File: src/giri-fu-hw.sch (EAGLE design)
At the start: 30 parts, among them IC1 ATMEGA168-20P, IC2 7805T, IC3 ULN2003AN, K1 G5V1, K2 G5V1, K3 G5V1, K4 G5V1, K5 G5V1, K6 G5V1, Q1 16MHz

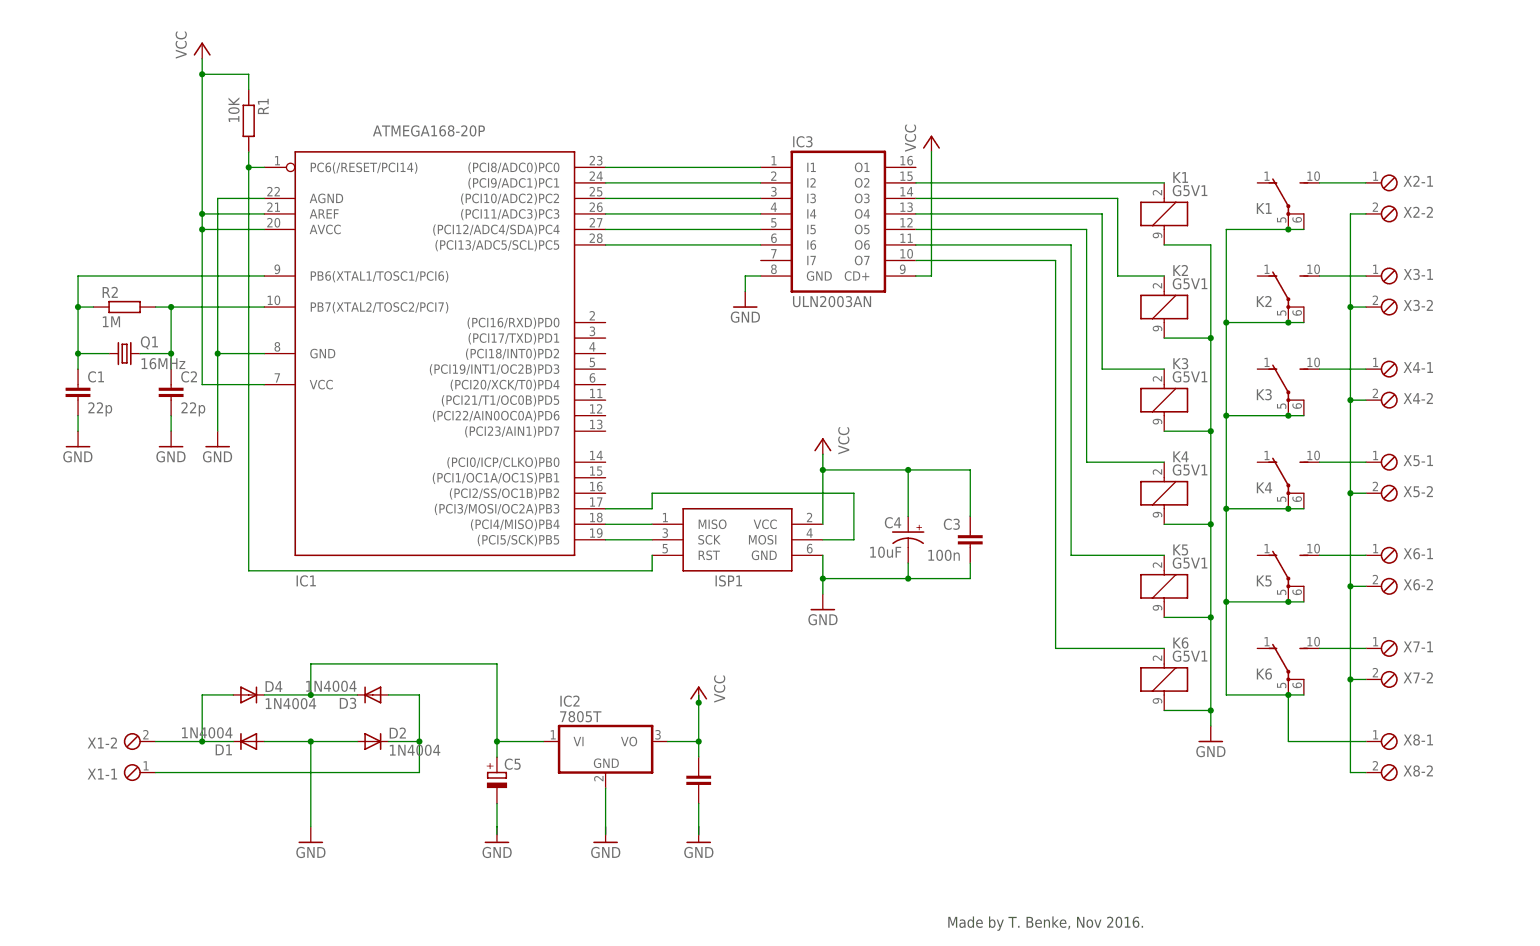
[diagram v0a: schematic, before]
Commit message: Add Schematics Add PCB board design Add top and bottom prints for manual PCB manufacturing Add partlist Add photo on the prototype board Add datasheet to the RYS-5 relay
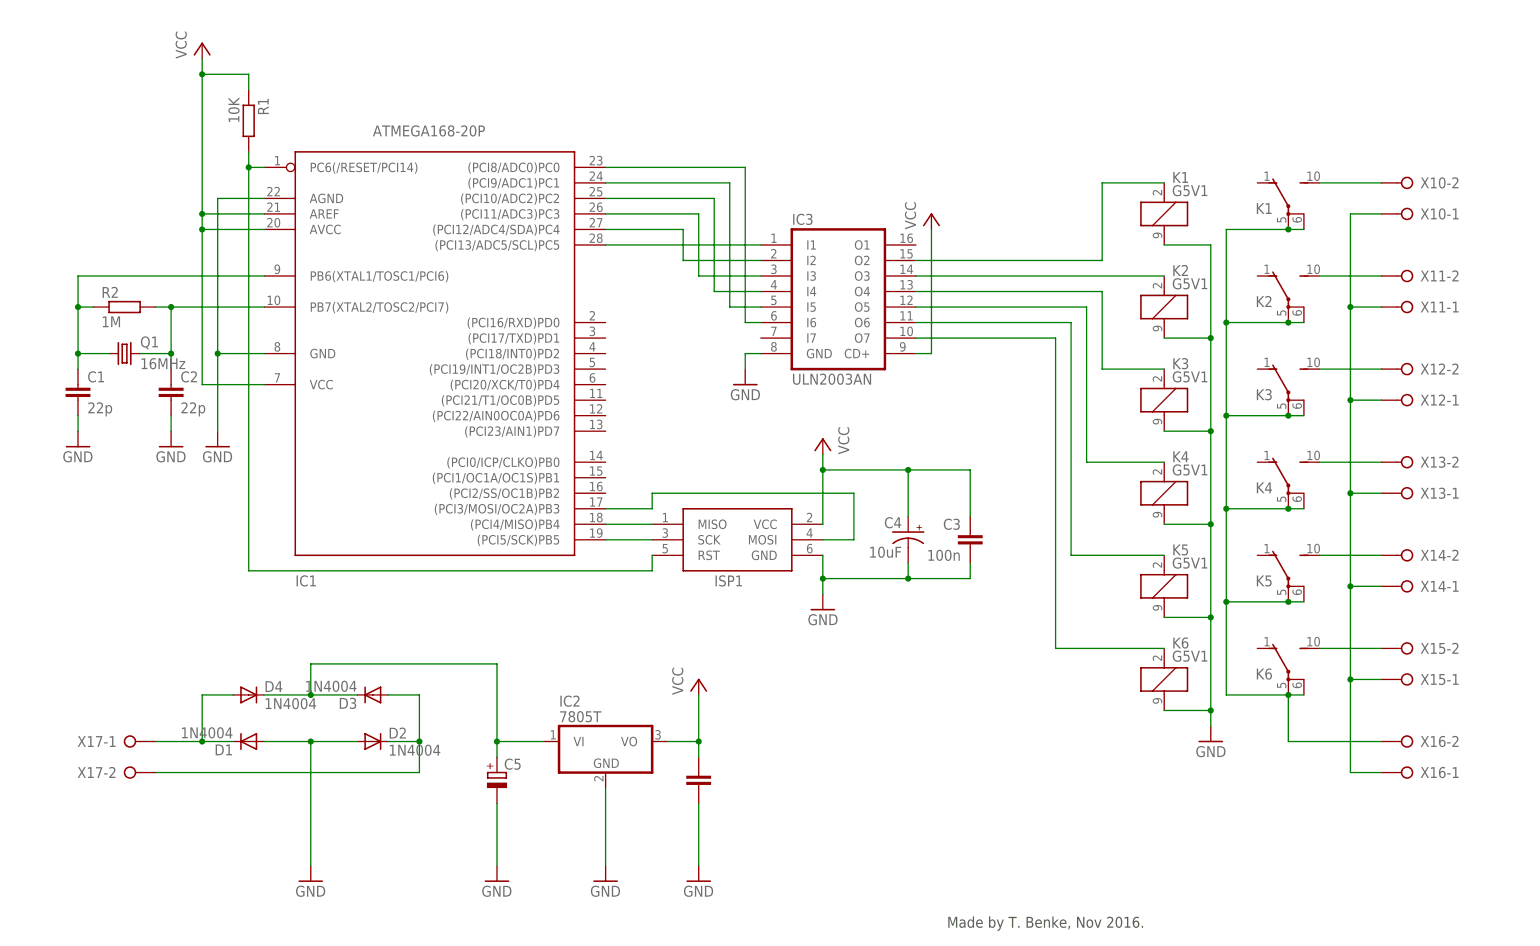
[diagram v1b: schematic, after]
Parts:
- removed X1, X2, X3, X4, X5, X6, X7, X8: (no value), con-phoenix-254:MPT2
- added X10, X11, X12, X13, X14, X15, X16, X17: (no value), con-wago-508:W237-02P
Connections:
- removed net N$24: IC2.GND
- removed net N$25: C5.-
- removed net N$26: IC2.VO
- removed net N$8: IC1.(PCI13/ADC5/SCL)PC5, IC3.I6
- net GND: now also C5.-, D1.A, D2.A, IC2.GND
- net N$1: now also IC3.I6; no longer IC3.I1
- net N$2: now also IC1.(PCI9/ADC1)PC1, IC3.I5; no longer D1.A, D2.A
- net N$22: now also X17-1.KL; no longer X1-2.1
- net N$23: now also X17-2.KL; no longer X1-1.1
- net N$28: now also X10-2.KL; no longer X2-1.1
- net N$29: now also X11-2.KL; no longer X3-1.1
- net N$3: now also X16-2.KL; no longer X8-1.1
- net N$30: now also X12-2.KL; no longer X4-1.1
- net N$31: now also X13-2.KL; no longer X5-1.1
- net N$32: now also X14-2.KL; no longer X6-1.1
- net N$33: now also X15-2.KL; no longer X7-1.1
- net N$35: now also X10-1.KL, X11-1.KL, X12-1.KL, X13-1.KL, X14-1.KL, X15-1.KL, X16-1.KL; no longer X2-2.1, X3-2.1, X4-2.1, X5-2.1, X6-2.1, X7-2.1, X8-2.1
- net N$4: now also IC1.(PCI10/ADC2)PC2, IC3.I4; no longer IC1.(PCI9/ADC1)PC1, IC3.I2
- net N$5: now also IC1.(PCI13/ADC5/SCL)PC5, IC3.I1; no longer IC1.(PCI10/ADC2)PC2, IC3.I3
- net N$6: now also IC3.I3; no longer IC3.I4
- net N$7: now also IC3.I2; no longer IC3.I5
- net VCC: now also IC2.VO
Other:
- moved on the sheet: IC3

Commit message: Rename inputs and outputs Regenerate dist artifacts
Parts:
- renumbered X10 to SWITCH_1, X11 to SWITCH_2, X12 to SWITCH_3, X13 to SWITCH_4, X14 to SWITCH_5, X15 to SWITCH_6, X16 to 24VAC_IN, X17 to 12VAC_IN
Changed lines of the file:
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@@
 <part name="C5" library="rcl" deviceset="CPOL-EU" device="E35-12AXIAL"/>
 <part name="C6" library="docu-dummy" deviceset="C" device=""/>
-<part name="X10" library="con-wago-508" deviceset="W237-02P" device=""/>
-<part name="X11" library="con-wago-508" deviceset="W237-02P" device=""/>
-<part name="X12" library="con-wago-508" deviceset="W237-02P" device=""/>
-<part name="X13" library="con-wago-508" deviceset="W237-02P" device=""/>
-<part name="X14" library="con-wago-508" deviceset="W237-02P" device=""/>
-<part name="X15" library="con-wago-508" deviceset="W237-02P" device=""/>
-<part name="X16" library="con-wago-508" deviceset="W237-02P" device=""/>
-<part name="X17" library="con-wago-508" deviceset="W237-02P" device=""/>
+<part name="SWITCH_1" library="con-wago-508" deviceset="W237-02P" device=""/>
+<part name="SWITCH_2" library="con-wago-508" deviceset="W237-02P" device=""/>
+<part name="SWITCH_3" library="con-wago-508" deviceset="W237-02P" device=""/>
+<part name="SWITCH_4" library="con-wago-508" deviceset="W237-02P" device=""/>
+<part name="SWITCH_5" library="con-wago-508" deviceset="W237-02P" device=""/>
+<part name="SWITCH_6" library="con-wago-508" deviceset="W237-02P" device=""/>
+<part name="24VAC_IN" library="con-wago-508" deviceset="W237-02P" device=""/>
+<part name="12VAC_IN" library="con-wago-508" deviceset="W237-02P" device=""/>
 <part name="GND7" library="supply1" deviceset="GND" device=""/>
 <part name="GND12" library="supply1" deviceset="GND" device=""/>
@@
 <instance part="C5" gate="G$1" x="88.9" y="45.72"/>
 <instance part="C6" gate="G$1" x="121.92" y="45.72"/>
-<instance part="X10" gate="-1" x="238.76" y="137.16" rot="R180"/>
-<instance part="X10" gate="-2" x="238.76" y="142.24" rot="R180"/>
-<instance part="X11" gate="-1" x="238.76" y="121.92" rot="R180"/>
-<instance part="X11" gate="-2" x="238.76" y="127" rot="R180"/>
-<instance part="X12" gate="-1" x="238.76" y="106.68" rot="R180"/>
-<instance part="X12" gate="-2" x="238.76" y="111.76" rot="R180"/>
-<instance part="X13" gate="-1" x="238.76" y="91.44" rot="R180"/>
-<instance part="X13" gate="-2" x="238.76" y="96.52" rot="R180"/>
-<instance part="X14" gate="-1" x="238.76" y="76.2" rot="R180"/>
-<instance part="X14" gate="-2" x="238.76" y="81.28" rot="R180"/>
-<instance part="X15" gate="-1" x="238.76" y="60.96" rot="R180"/>
-<instance part="X15" gate="-2" x="238.76" y="66.04" rot="R180"/>
-<instance part="X16" gate="-1" x="238.76" y="45.72" rot="R180"/>
-<instance part="X16" gate="-2" x="238.76" y="50.8" rot="R180"/>
-<instance part="X17" gate="-1" x="27.94" y="50.8"/>
-<instance part="X17" gate="-2" x="27.94" y="45.72"/>
+<instance part="SWITCH_1" gate="-1" x="238.76" y="137.16" rot="R180"/>
+<instance part="SWITCH_1" gate="-2" x="238.76" y="142.24" rot="R180"/>
+<instance part="SWITCH_2" gate="-1" x="238.76" y="121.92" rot="R180"/>
+<instance part="SWITCH_2" gate="-2" x="238.76" y="127" rot="R180"/>
+<instance part="SWITCH_3" gate="-1" x="238.76" y="106.68" rot="R180"/>
+<instance part="SWITCH_3" gate="-2" x="238.76" y="111.76" rot="R180"/>
+<instance part="SWITCH_4" gate="-1" x="238.76" y="91.44" rot="R180"/>
+<instance part="SWITCH_4" gate="-2" x="238.76" y="96.52" rot="R180"/>
+<instance part="SWITCH_5" gate="-1" x="238.76" y="76.2" rot="R180"/>
+<instance part="SWITCH_5" gate="-2" x="238.76" y="81.28" rot="R180"/>
+<instance part="SWITCH_6" gate="-1" x="238.76" y="60.96" rot="R180"/>
+<instance part="SWITCH_6" gate="-2" x="238.76" y="66.04" rot="R180"/>
+<instance part="24VAC_IN" gate="-1" x="238.76" y="45.72" rot="R180"/>
+<instance part="24VAC_IN" gate="-2" x="238.76" y="50.8" rot="R180"/>
+<instance part="12VAC_IN" gate="-1" x="27.94" y="50.8"/>
+<instance part="12VAC_IN" gate="-2" x="27.94" y="45.72"/>
 <instance part="GND7" gate="1" x="106.68" y="27.94"/>
 <instance part="GND12" gate="1" x="88.9" y="27.94"/>
@@
 <wire x1="218.44" y1="50.8" x2="218.44" y2="58.42" width="0.1524" layer="91"/>
 <junction x="218.44" y="88.9"/>
-<pinref part="X16" gate="-2" pin="KL"/>
+<pinref part="24VAC_IN" gate="-2" pin="KL"/>
 <wire x1="233.68" y1="50.8" x2="218.44" y2="50.8" width="0.1524" layer="91"/>
 </segment>
@@
 <pinref part="D1" gate="1" pin="C"/>
 <wire x1="45.72" y1="50.8" x2="40.64" y2="50.8" width="0.1524" layer="91"/>
-<pinref part="X17" gate="-1" pin="KL"/>
+<pinref part="12VAC_IN" gate="-1" pin="KL"/>
 <wire x1="40.64" y1="50.8" x2="33.02" y2="50.8" width="0.1524" layer="91"/>
 <junction x="40.64" y="50.8"/>
@@
 <wire x1="71.12" y1="50.8" x2="76.2" y2="50.8" width="0.1524" layer="91"/>
 <junction x="76.2" y="50.8"/>
-<pinref part="X17" gate="-2" pin="KL"/>
+<pinref part="12VAC_IN" gate="-2" pin="KL"/>
 <wire x1="76.2" y1="45.72" x2="33.02" y2="45.72" width="0.1524" layer="91"/>
 </segment>
@@
 <segment>
 <wire x1="228.6" y1="137.16" x2="228.6" y2="121.92" width="0.1524" layer="91"/>
-<pinref part="X16" gate="-1" pin="KL"/>
+<pinref part="24VAC_IN" gate="-1" pin="KL"/>
 <wire x1="228.6" y1="121.92" x2="228.6" y2="106.68" width="0.1524" layer="91"/>
 <wire x1="228.6" y1="106.68" x2="228.6" y2="91.44" width="0.1524" layer="91"/>
@@
 <wire x1="228.6" y1="60.96" x2="228.6" y2="45.72" width="0.1524" layer="91"/>
 <wire x1="233.68" y1="45.72" x2="228.6" y2="45.72" width="0.1524" layer="91"/>
-<pinref part="X15" gate="-1" pin="KL"/>
+<pinref part="SWITCH_6" gate="-1" pin="KL"/>
 <wire x1="233.68" y1="60.96" x2="228.6" y2="60.96" width="0.1524" layer="91"/>
-<pinref part="X14" gate="-1" pin="KL"/>
+<pinref part="SWITCH_5" gate="-1" pin="KL"/>
 <wire x1="233.68" y1="76.2" x2="228.6" y2="76.2" width="0.1524" layer="91"/>
-<pinref part="X13" gate="-1" pin="KL"/>
+<pinref part="SWITCH_4" gate="-1" pin="KL"/>
 <wire x1="233.68" y1="91.44" x2="228.6" y2="91.44" width="0.1524" layer="91"/>
-<pinref part="X12" gate="-1" pin="KL"/>
+<pinref part="SWITCH_3" gate="-1" pin="KL"/>
 <wire x1="233.68" y1="106.68" x2="228.6" y2="106.68" width="0.1524" layer="91"/>
-<pinref part="X11" gate="-1" pin="KL"/>
+<pinref part="SWITCH_2" gate="-1" pin="KL"/>
 <wire x1="233.68" y1="121.92" x2="228.6" y2="121.92" width="0.1524" layer="91"/>
-<pinref part="X10" gate="-1" pin="KL"/>
+<pinref part="SWITCH_1" gate="-1" pin="KL"/>
 <wire x1="233.68" y1="137.16" x2="228.6" y2="137.16" width="0.1524" layer="91"/>
 <junction x="228.6" y="60.96"/>
@@
 <net name="N$28" class="0">
 <segment>
-<pinref part="X10" gate="-2" pin="KL"/>
+<pinref part="SWITCH_1" gate="-2" pin="KL"/>
 <pinref part="K1" gate="2" pin="S"/>
 <wire x1="233.68" y1="142.24" x2="223.52" y2="142.24" width="0.1524" layer="91"/>
@@
 <net name="N$29" class="0">
 <segment>
-<pinref part="X11" gate="-2" pin="KL"/>
+<pinref part="SWITCH_2" gate="-2" pin="KL"/>
 <pinref part="K2" gate="2" pin="S"/>
 <wire x1="233.68" y1="127" x2="223.52" y2="127" width="0.1524" layer="91"/>
@@
 <net name="N$30" class="0">
 <segment>
-<pinref part="X12" gate="-2" pin="KL"/>
+<pinref part="SWITCH_3" gate="-2" pin="KL"/>
 <pinref part="K3" gate="2" pin="S"/>
 <wire x1="233.68" y1="111.76" x2="223.52" y2="111.76" width="0.1524" layer="91"/>
@@
 <net name="N$31" class="0">
 <segment>
-<pinref part="X13" gate="-2" pin="KL"/>
+<pinref part="SWITCH_4" gate="-2" pin="KL"/>
 <pinref part="K4" gate="2" pin="S"/>
 <wire x1="233.68" y1="96.52" x2="223.52" y2="96.52" width="0.1524" layer="91"/>
@@
 <net name="N$32" class="0">
 <segment>
-<pinref part="X14" gate="-2" pin="KL"/>
+<pinref part="SWITCH_5" gate="-2" pin="KL"/>
 <pinref part="K5" gate="2" pin="S"/>
 <wire x1="233.68" y1="81.28" x2="223.52" y2="81.28" width="0.1524" layer="91"/>
@@
 <net name="N$33" class="0">
 <segment>
-<pinref part="X15" gate="-2" pin="KL"/>
+<pinref part="SWITCH_6" gate="-2" pin="KL"/>
 <pinref part="K6" gate="2" pin="S"/>
 <wire x1="233.68" y1="66.04" x2="223.52" y2="66.04" width="0.1524" layer="91"/>

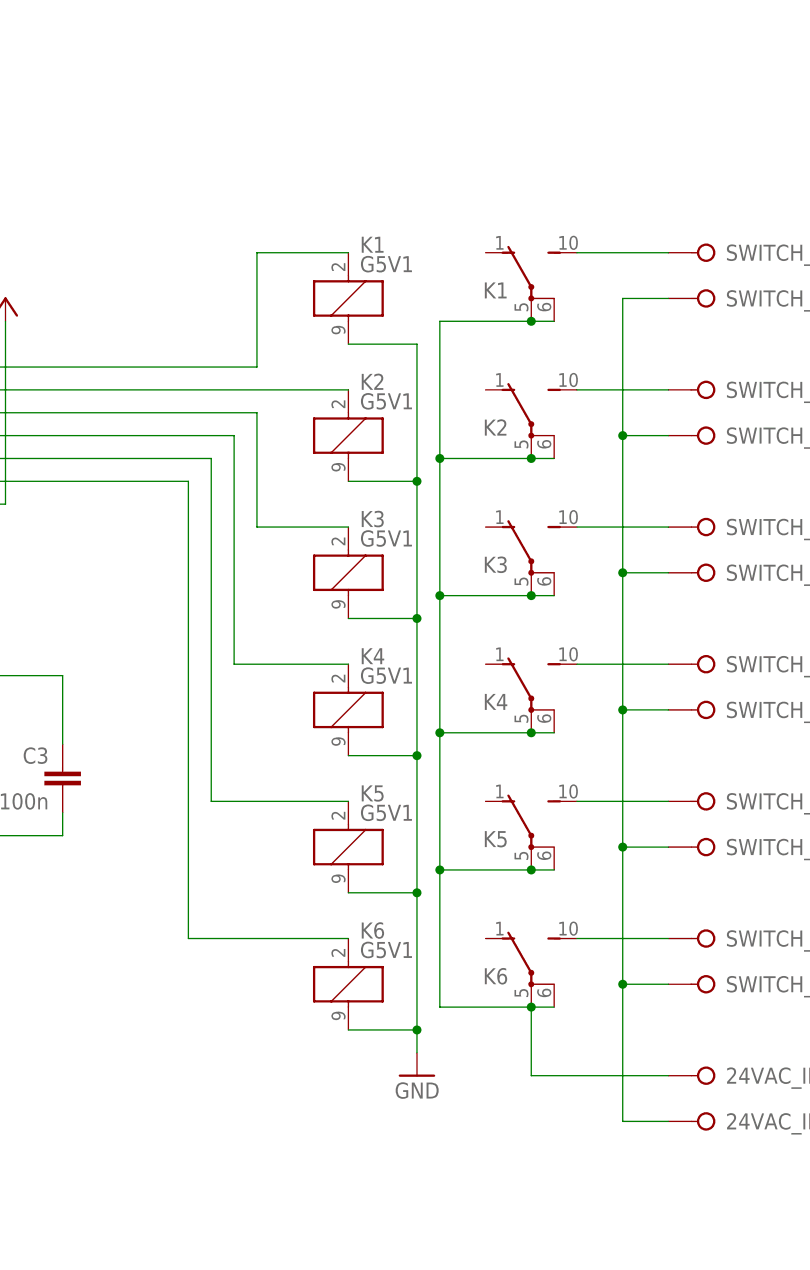
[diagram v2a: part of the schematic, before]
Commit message: Change the relay driver endpoint from ground to vcc
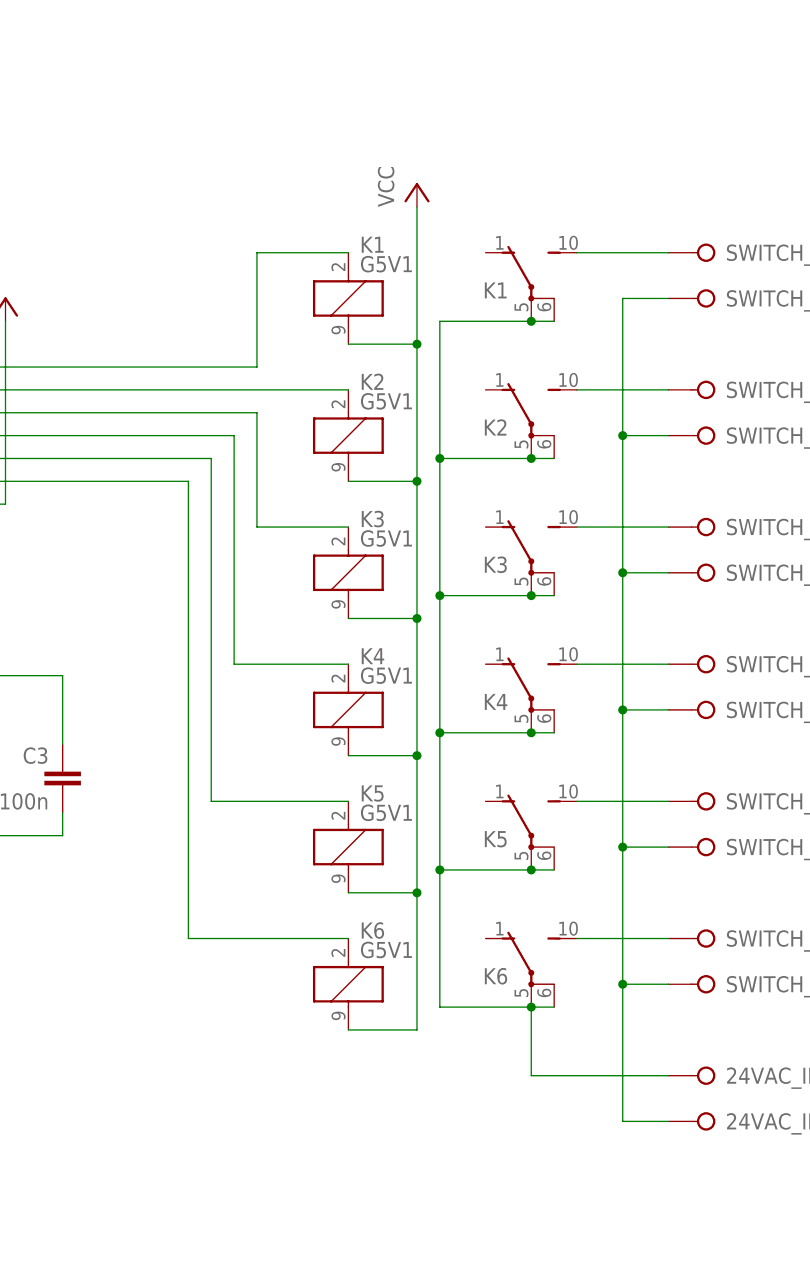
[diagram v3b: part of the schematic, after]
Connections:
- removed net VCC: C3.1, C4.+, IC1.AREF, IC1.AVCC, IC1.VCC, IC2.VO, IC3.CD+, ISP1.VCC, R1.1
- new net N$8: C3.1, C4.+, IC1.AREF, IC1.AVCC, IC1.VCC, IC2.VO, IC3.CD+, ISP1.VCC, K11.2, K21.2, K31.2, K41.2, K51.2, K61.2, R1.1
- net GND: no longer K11.2, K21.2, K31.2, K41.2, K51.2, K61.2
